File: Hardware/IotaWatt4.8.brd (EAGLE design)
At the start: 87 x 67.9 mm, 53 parts

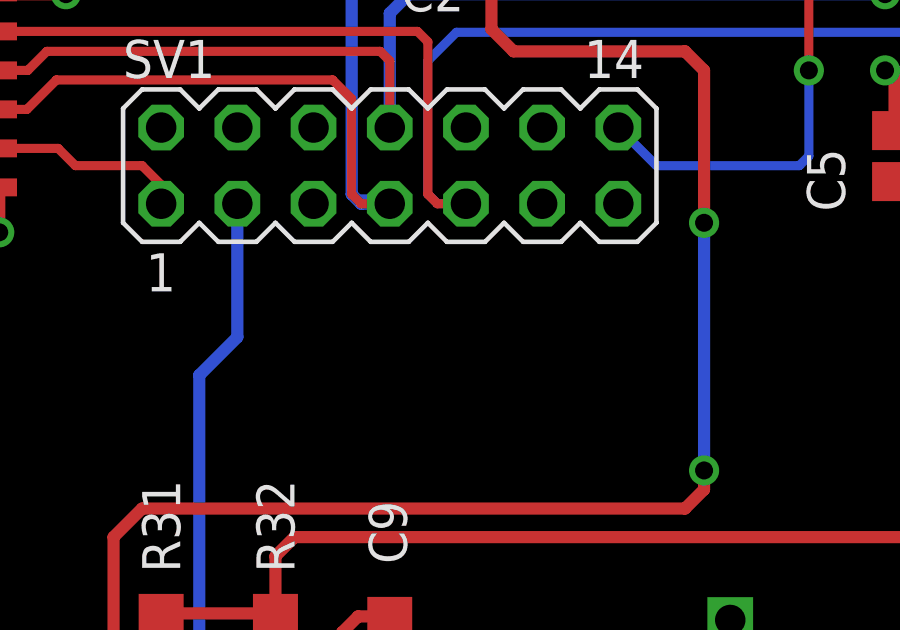
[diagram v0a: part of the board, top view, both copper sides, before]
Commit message: SPI termination resistor positions
added SPI termination resistor positions
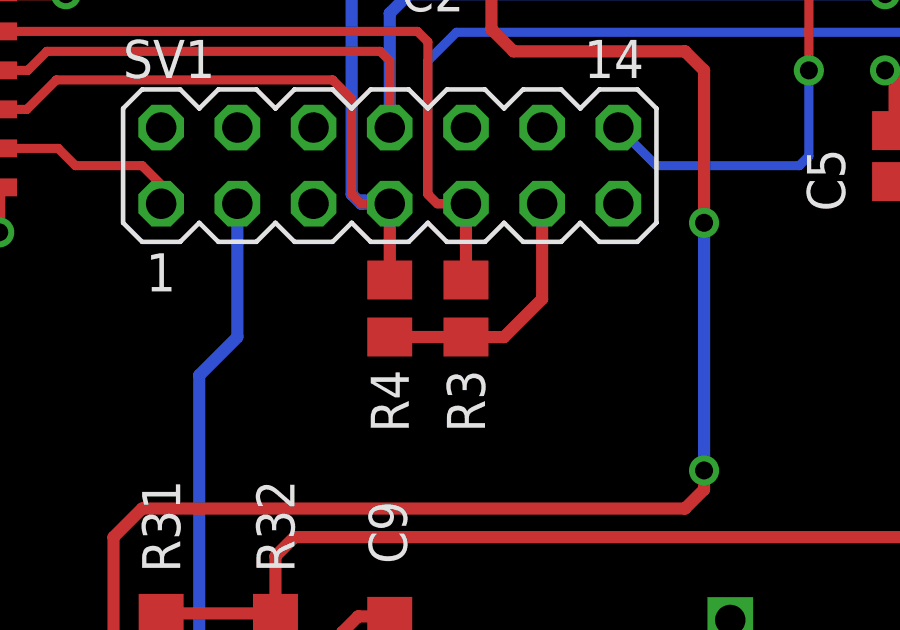
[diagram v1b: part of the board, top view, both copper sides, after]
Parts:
- added R3, R4: 330, resistor:R0805
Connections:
- net GND: now also R3.1, R4.1
- net MOSI: now also R4.2
- net SCLK: now also R3.2
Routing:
- net GND: track 45.0 -> 53.8 mm
- net SCLK: track 45.6 -> 48.1 mm
- net MOSI: track 48.3 -> 50.9 mm
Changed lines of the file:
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@@
 <attribute name="NAME" x="34.925" y="39.6875" size="1.27" layer="25" rot="R270"/>
+</element>
+<element name="R3" library="resistor" package="R0805" value="330" x="41.91" y="45.4025" smashed="yes" rot="R90">
+<attribute name="NAME" x="42.545" y="41.275" size="1.27" layer="25" rot="R90"/>
+</element>
+<element name="R4" library="resistor" package="R0805" value="330" x="39.37" y="45.4025" smashed="yes" rot="R90">
+<attribute name="NAME" x="40.005" y="41.275" size="1.27" layer="25" rot="R90"/>
 </element>
 </elements>
@@
 <wire x1="26.195" y1="55.94" x2="26.255" y2="55.88" width="0.4064" layer="1"/>
 <wire x1="26.255" y1="55.88" x2="28.575" y2="55.88" width="0.4064" layer="1"/>
+<wire x1="58.895" y1="61.4375" x2="58.42" y2="61.9125" width="0.3048" layer="1"/>
+<contactref element="R3" pad="1"/>
+<contactref element="R4" pad="1"/>
 <wire x1="36.83" y1="60.325" x2="37.405" y2="60.33" width="0" layer="19" extent="1-1"/>
-<wire x1="58.895" y1="61.4375" x2="58.42" y2="61.9125" width="0.3048" layer="1"/>
+<wire x1="44.45" y1="48.895" x2="44.45" y2="45.72" width="0.4064" layer="1"/>
+<wire x1="44.45" y1="45.72" x2="43.18" y2="44.45" width="0.4064" layer="1"/>
+<wire x1="43.18" y1="44.45" x2="41.9125" y2="44.45" width="0.4064" layer="1"/>
+<wire x1="41.9125" y1="44.45" x2="41.91" y2="44.4525" width="0.4064" layer="1"/>
+<wire x1="41.91" y1="44.4525" x2="39.37" y2="44.4525" width="0.4064" layer="1"/>
 </signal>
 <signal name="ADC1">
@@
 <wire x1="38.1" y1="49.2125" x2="38.4175" y2="48.895" width="0.4064" layer="16"/>
 <wire x1="38.4175" y1="48.895" x2="39.37" y2="48.895" width="0.4064" layer="16"/>
+<contactref element="R4" pad="2"/>
+<wire x1="39.37" y1="46.3525" x2="39.37" y2="48.895" width="0.4064" layer="1"/>
 </signal>
 <signal name="SCLK">
@@
 <wire x1="40.64" y1="49.2125" x2="40.9575" y2="48.895" width="0.3048" layer="16"/>
 <wire x1="40.9575" y1="48.895" x2="41.91" y2="48.895" width="0.3048" layer="16"/>
+<contactref element="R3" pad="2"/>
+<wire x1="41.91" y1="46.3525" x2="41.91" y2="48.895" width="0.4064" layer="1"/>
 </signal>
 <signal name="3V3">

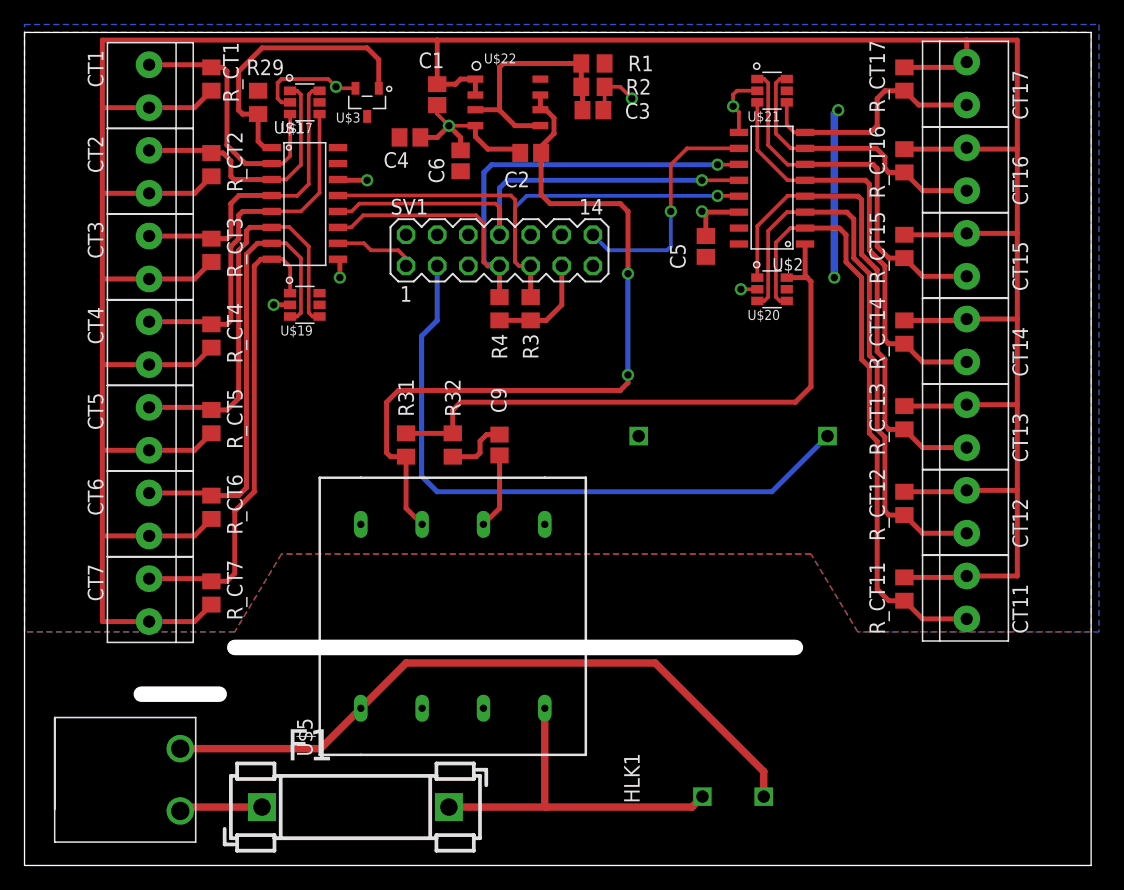
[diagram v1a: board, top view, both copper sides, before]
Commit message: mechanical fitting
moved the clamp positions such that they should fit unmodified.
Added silkscreen signal names for the power board ribbon connector, improved 3V3 connection on IO Board
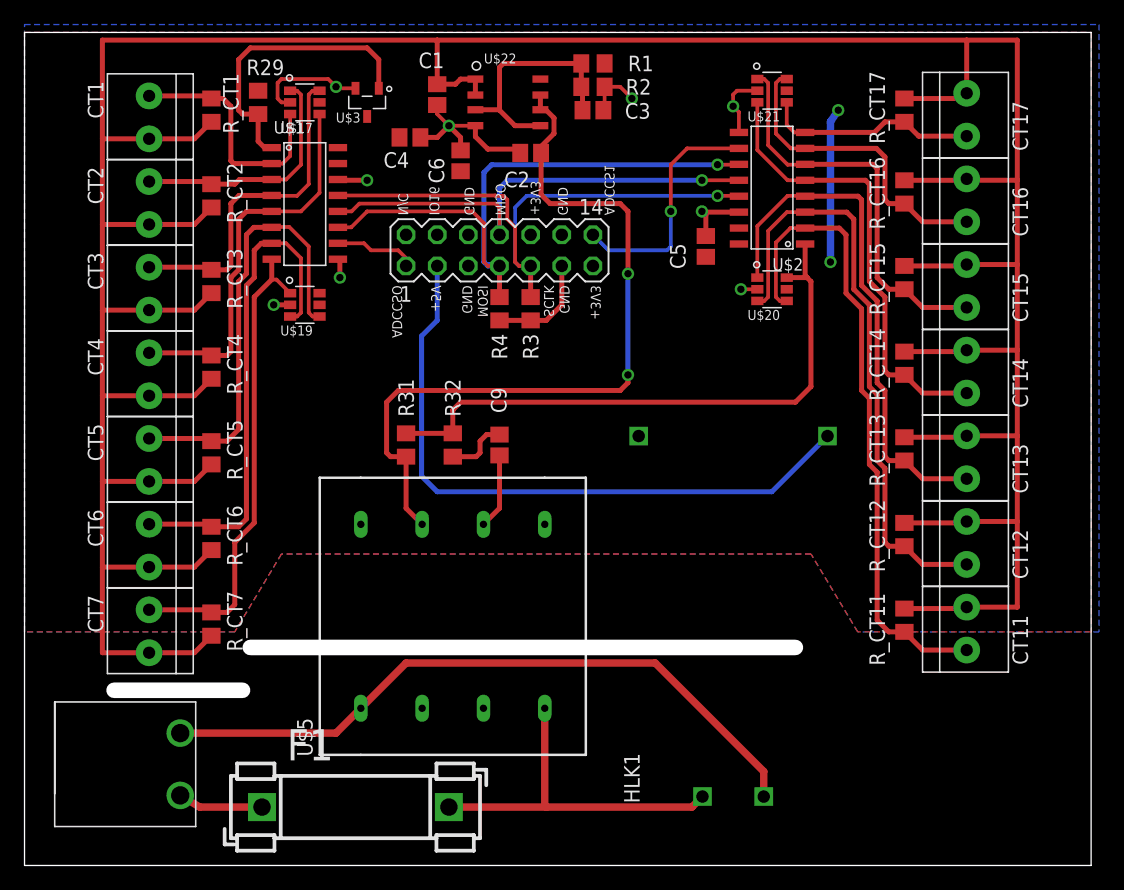
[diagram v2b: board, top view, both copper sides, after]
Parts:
- moved CT16 2.54 mm to (77.5, 54.3)
- moved R_CT1 2.54 mm to (15.9, 61.6)
- moved R_CT13 2.54 mm to (72.4, 34.0)
- moved R_CT17 2.54 mm to (72.4, 61.6)
- moved R_CT7 2.54 mm to (15.9, 19.7)
- moved CT1 2.54 mm to (10.8, 61.0)
- moved CT11 2.54 mm to (77.5, 19.4)
- moved CT12 2.54 mm to (77.5, 26.4)
- moved CT13 2.54 mm to (77.5, 33.3)
- moved CT14 2.54 mm to (77.5, 40.3)
- moved CT15 2.54 mm to (77.5, 47.3)
- moved CT17 2.54 mm to (77.5, 61.3)
- moved CT2 2.54 mm to (10.8, 54.0)
- moved CT3 2.54 mm to (10.8, 47.0)
- moved CT4 2.54 mm to (10.8, 40.0)
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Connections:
- net 3V3: now also SV1.10
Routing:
- net BIAS: track 303.4 -> 311.1 mm
- net ADC12: track 46.5 -> 49.1 mm
- net ADC11: track 50.1 -> 52.7 mm
- net ADC3: track 24.8 -> 27.3 mm
- net ADC16: track 23.2 -> 25.7 mm
- net ADC15: track 30.5 -> 33.0 mm
- net ADC14: track 34.8 -> 37.4 mm
- net ADC13: track 40.5 -> 43.0 mm
- net ADC5: track 34.0 -> 36.3 mm
- net ADC17: track 20.0 -> 17.6 mm
- net ADC6: track 38.1 -> 40.5 mm
- net ADC4: track 29.5 -> 31.9 mm
- net ADC1: track 22.1 -> 20.1 mm
- net ADC2: track 21.3 -> 19.9 mm
- net 3V3: track 13.8 -> 12.6 mm
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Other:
- outline, holes or cut-outs redrawn
- board text added: "+3V3"
- board text added: "+5V"
- board text added: "ADCCS1"
- board text added: "ADCCSO"
- board text added: "GND"
- board text added: "IO16"
- board text added: "MISO"
- board text added: "MOSI"
- board text added: "N/C"
- board text added: "SCLK"
